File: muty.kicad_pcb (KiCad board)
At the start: 2 copper layers, 39 parts, among them J1 Conn_ARM_SWD_TagConnect_TC2030, J2 Conn_02x05_Odd_Even, U1 STM32F439ZITx, Y1 NX3215SA-32.768KHZ-EXS00A-MU0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, Y2 ECS-2520MVQ-160-CN-TR

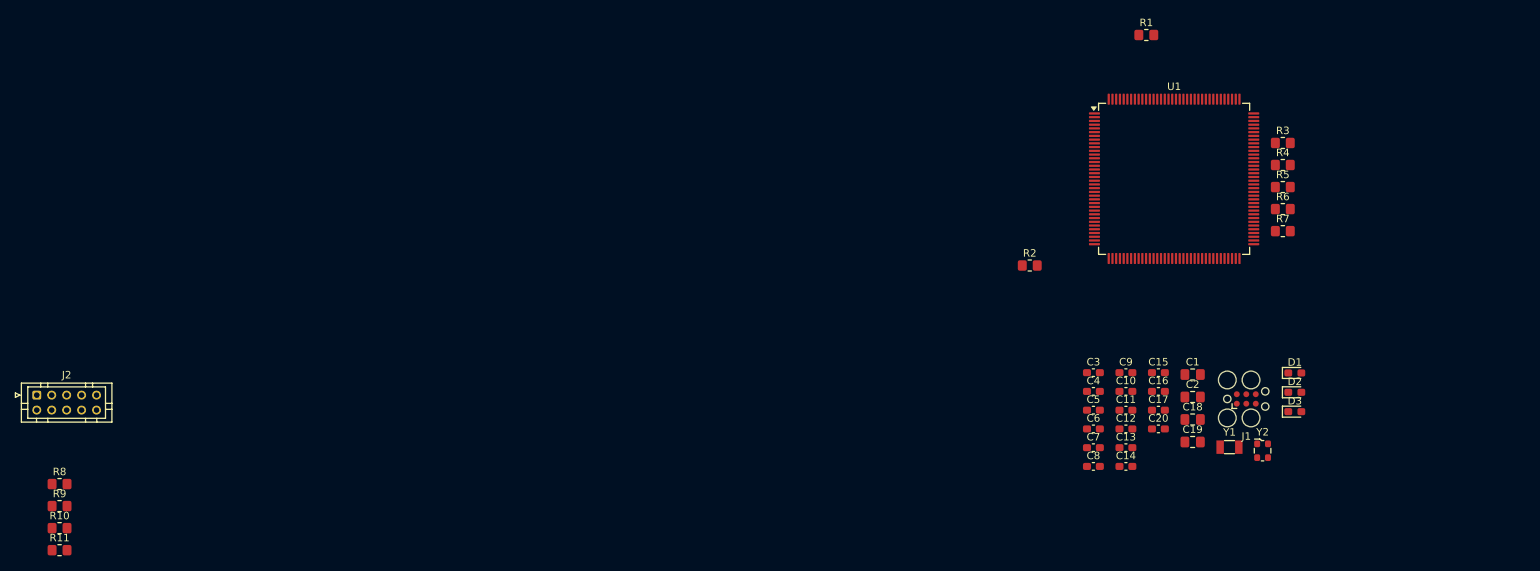
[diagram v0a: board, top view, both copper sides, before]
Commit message: feat: add bq25887 connector
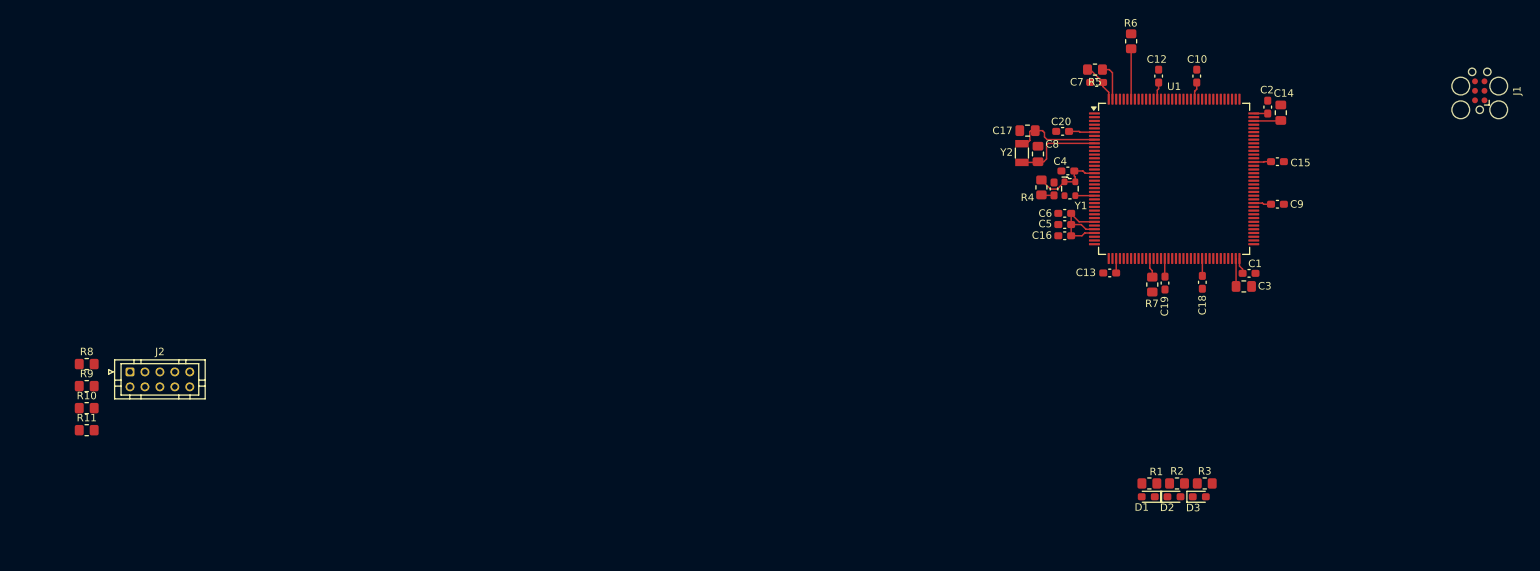
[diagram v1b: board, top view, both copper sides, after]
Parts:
- R11: value 900K -> 4,7K
- R9: value 4,7K -> 900K
- moved C10 53.1 mm to (207.8, 78.8), turned to -90 degrees
- moved J1 51.7 mm to (245.7, 80.8), turned to 90 degrees
- moved C12 50.5 mm to (202.8, 78.8), turned to -90 degrees
- moved C7 49.0 mm to (194.4, 79.7)
- moved Y2 48.2 mm to (184.4, 89.2), turned to -90 degrees
- moved C15 47.6 mm to (218.7, 90.3), turned to 180 degrees
- moved C14 45.6 mm to (219.1, 83.8), turned to -90 degrees
- moved C2 44.8 mm to (217.3, 83.0), turned to -90 degrees
- moved Y1 43.5 mm to (190.9, 93.9)
- moved R1 43.5 mm to (201.5, 133.4), turned to 180 degrees
- moved C17 41.9 mm to (185.2, 86.2)
- moved C20 39.5 mm to (189.9, 86.2)
- moved R2 39.4 mm to (205.2, 133.4)
- moved C9 37.0 mm to (218.7, 96.0), turned to 180 degrees
- moved C8 36.1 mm to (186.6, 89.3), turned to -90 degrees
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- renumbered C6 to C1, C14 to C10, C20 to C11, C7 to C12, C15 to C13, C19 to C14, C8 to C15, C2 to C17, C9 to C18, C10 to C19, C11 to C2, C17 to C20, C18 to C3, C3 to C4, C12 to C5, C4 to C6, C13 to C7, C1 to C8, C5 to C9, R5 to R1, R6 to R2, R7 to R3, R3 to R4, R4 to R5, R1 to R6, R2 to R7, Y2 to Y1, Y1 to Y2
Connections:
- R10 pad 2: BQ25887RGE_INT -> BQ25887RGE_SCL
- R11 pad 1: BQ25887RGE_CD -> +3.3V
- R11 pad 2: GND -> BQ25887RGE_INT
- R9 pad 1: +3.3V -> BQ25887RGE_CD
- R9 pad 2: BQ25887RGE_SCL -> GND
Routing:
- net +3.3V: track 0.00 -> 51.9 mm
- net RCC_LSE_OUT: track 0.00 -> 12.0 mm
- net RCC_LSE_IN: track 0.00 -> 12.0 mm
- net MCU_BOOT0: track 0.00 -> 6.75 mm
- net MCU_PDR_ON: track 0.00 -> 5.05 mm
- net VCAP1: track 0.00 -> 3.76 mm
- net VCAP2: track 0.00 -> 3.64 mm
- net RCC_HSE_IN: track 0.00 -> 2.67 mm
- net MCU_BOOT1: track 0.00 -> 2.62 mm
- net SWNRST: track 0.00 -> 1.72 mm
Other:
- copper layers 2 -> 4

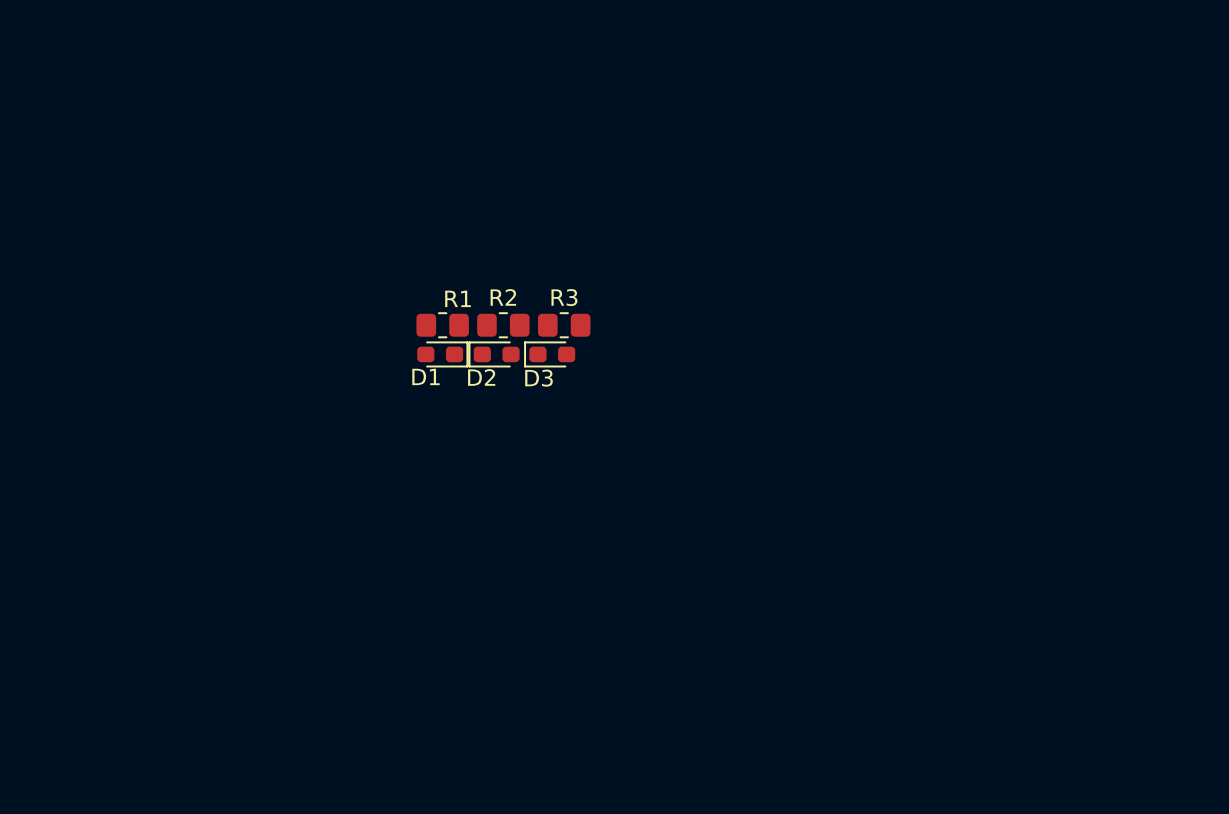
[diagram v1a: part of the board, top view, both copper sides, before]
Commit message: feat: add bno085+bme280
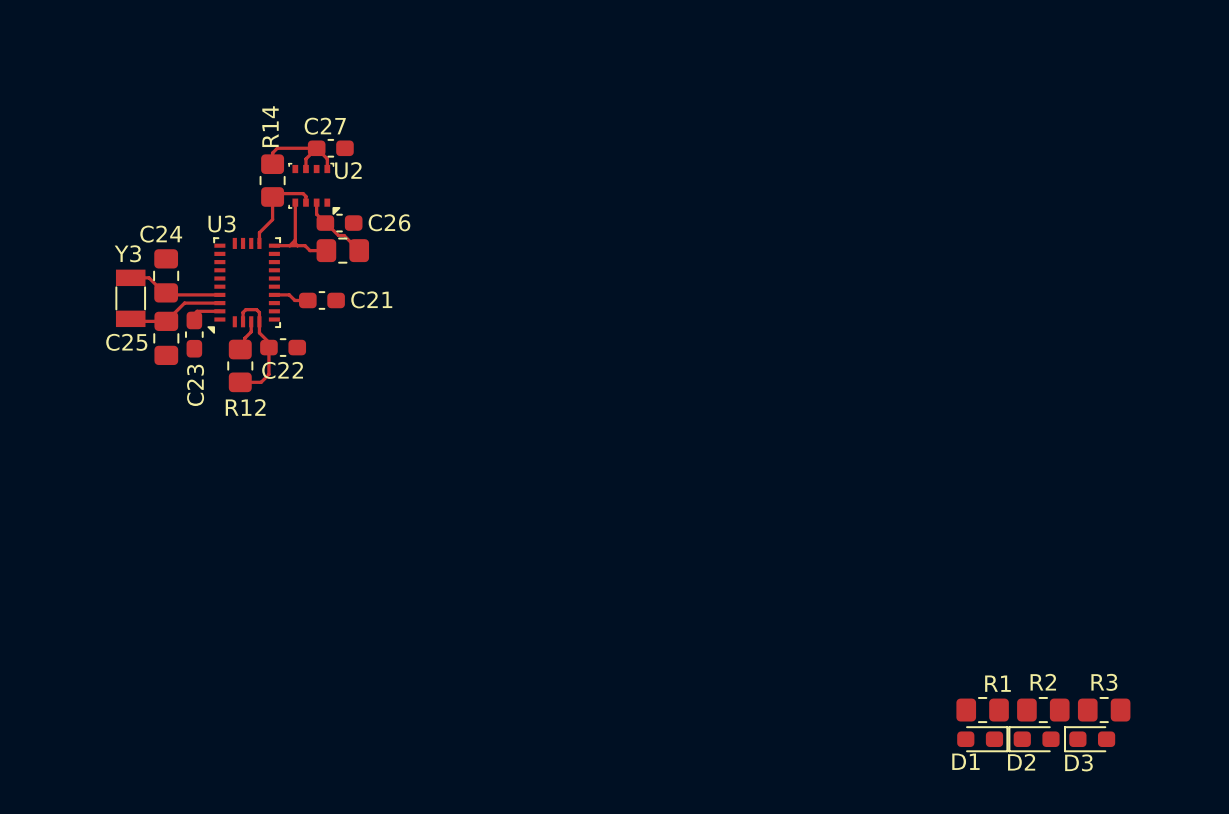
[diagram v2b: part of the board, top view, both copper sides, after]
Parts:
- added C21: 100nF, Capacitor_SMD:C_0603_1608Metric_Pad1.08x0.95mm_HandSolder, F.Cu at (194.2, 131.9)
- added C22: 100nF, Capacitor_SMD:C_0603_1608Metric_Pad1.08x0.95mm_HandSolder, F.Cu at (191.8, 134.7)
- added C23: 100nF, Capacitor_SMD:C_0603_1608Metric_Pad1.08x0.95mm_HandSolder, F.Cu at (186.4, 133.9)
- added C24: 22pF, Capacitor_SMD:C_0805_2012Metric_Pad1.18x1.45mm_HandSolder, F.Cu at (184.7, 130.4)
- added C25: 22pF, Capacitor_SMD:C_0805_2012Metric_Pad1.18x1.45mm_HandSolder, F.Cu at (184.7, 134.2)
- added C26: 100nF, Capacitor_SMD:C_0603_1608Metric_Pad1.08x0.95mm_HandSolder, F.Cu at (195.2, 127.1)
- added C27: 100nF, Capacitor_SMD:C_0603_1608Metric_Pad1.08x0.95mm_HandSolder, F.Cu at (194.7, 122.6)
- added R12: 10K, Resistor_SMD:R_0805_2012Metric_Pad1.20x1.40mm_HandSolder, F.Cu at (189.2, 135.8)
- added R13: 4,7K, Resistor_SMD:R_0805_2012Metric_Pad1.20x1.40mm_HandSolder, F.Cu at (195.4, 128.8)
- added R14: 4,7K, Resistor_SMD:R_0805_2012Metric_Pad1.20x1.40mm_HandSolder, F.Cu at (191.1, 124.5)
- added U2: BME280, Package_LGA:Bosch_LGA-8_2.5x2.5mm_P0.65mm_ClockwisePinNumbering, F.Cu at (193.5, 124.9)
- added U3: BNO085, Package_LGA:LGA-28_5.2x3.8mm_P0.5mm, F.Cu at (189.6, 130.8)
- added Y3: NX3215SA-32.768KHZ-EXS00A-MU00525, Crystal:Crystal_SMD_3215-2Pin_3.2x1.5mm, F.Cu at (182.5, 131.7)
- moved D1 40.4 mm to (234.3, 158.6)
- moved D3 40.4 mm to (241.1, 158.6)
- moved R1 40.4 mm to (234.4, 156.8)
- moved R3 40.4 mm to (241.8, 156.8)
- moved D2 40.4 mm to (237.7, 158.6)
- moved R2 40.4 mm to (238.1, 156.8)
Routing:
- net +3.3V: track 51.9 -> 72.4 mm
- net Net-(U2-SCK): track 0.00 -> 6.77 mm
- net Net-(U3-XIN32): track 0.00 -> 5.96 mm
- net Net-(U3-XOUT32): track 0.00 -> 5.87 mm
- net Net-(U2-SDI): track 0.00 -> 5.76 mm
- net Net-(U3-CAP): track 0.00 -> 2.18 mm
- net BNO085_BOOTN: track 0.00 -> 1.97 mm

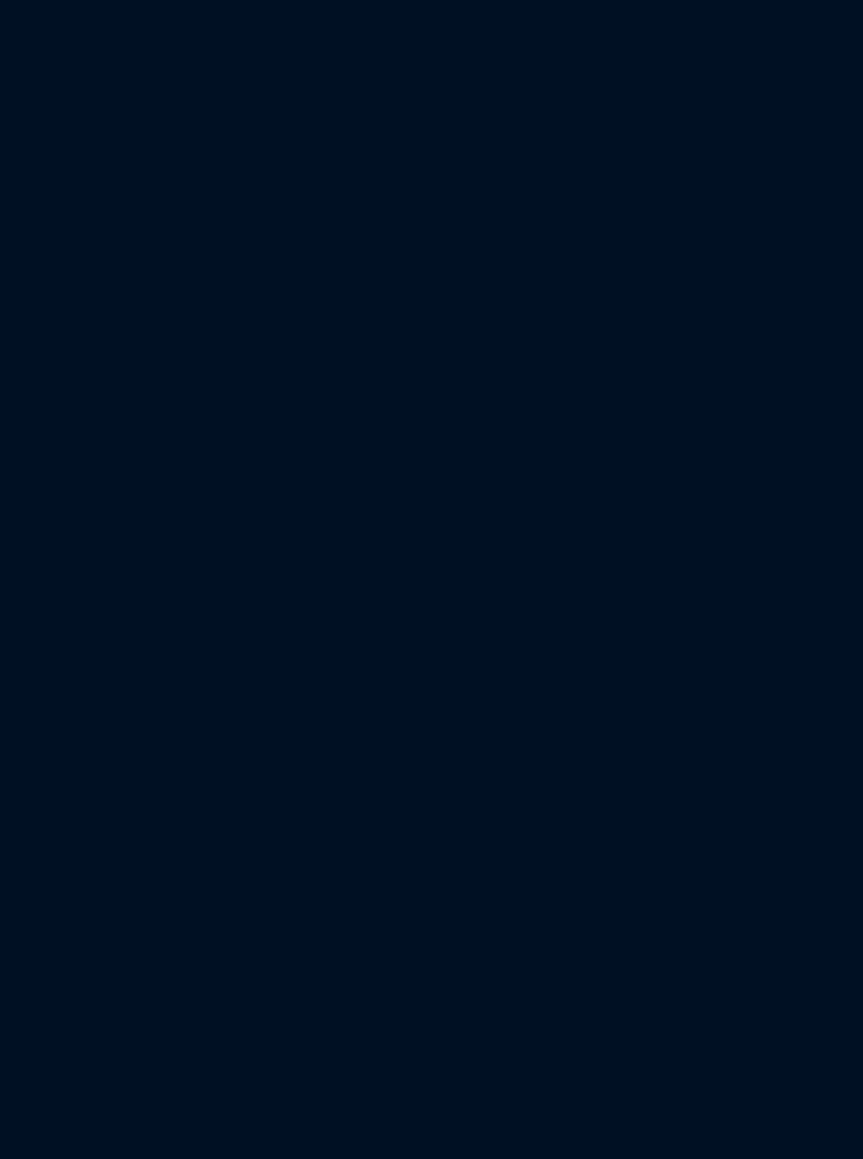
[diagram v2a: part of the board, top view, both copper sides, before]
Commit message: feat: add tb6612fng
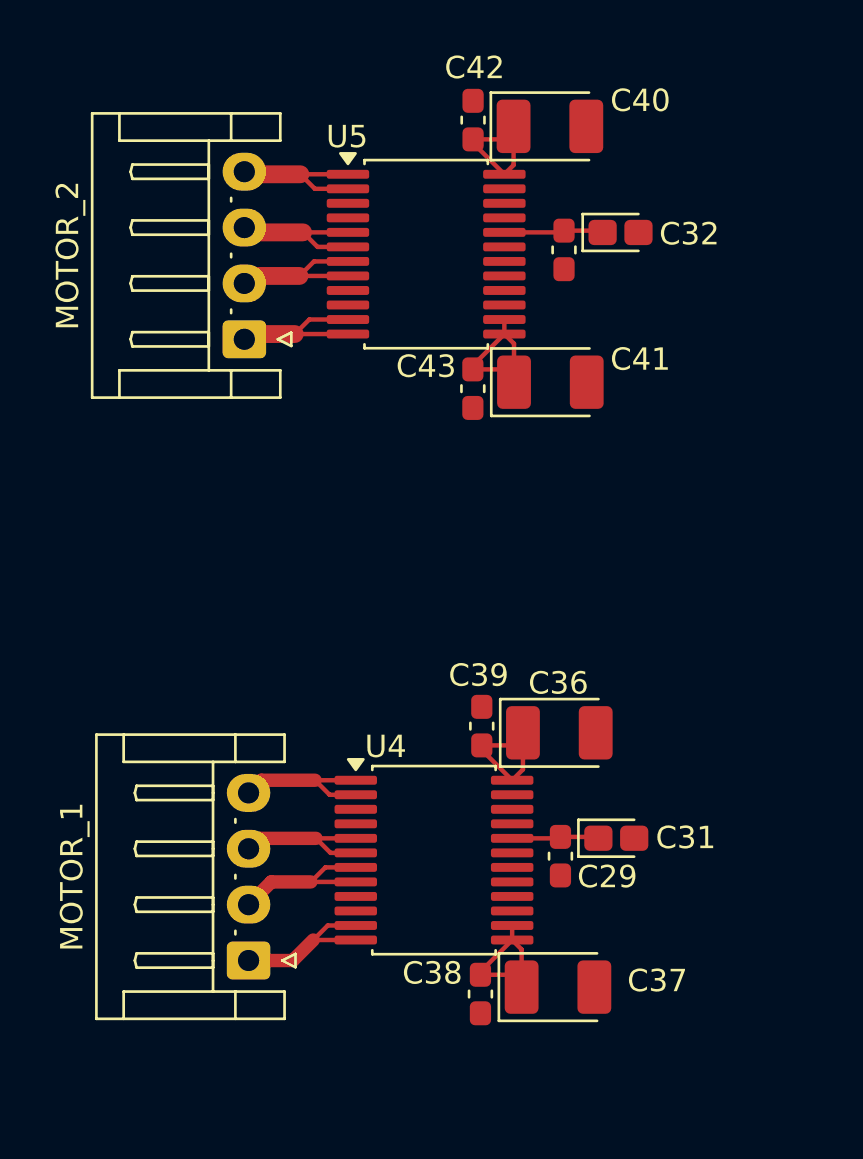
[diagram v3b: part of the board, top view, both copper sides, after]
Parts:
- added C29: 0.1μF, Capacitor_SMD:C_0603_1608Metric_Pad1.08x0.95mm_HandSolder, F.Cu at (46.3, 76.9)
- added C31: 10μF 10V, Capacitor_Tantalum_SMD:CP_EIA-1608-10_AVX-L_HandSolder, F.Cu at (48.8, 76.1)
- added C32: 10μF 10V, Capacitor_Tantalum_SMD:CP_EIA-1608-10_AVX-L_HandSolder, F.Cu at (49.0, 49.0)
- added C35: 0.1μF, Capacitor_SMD:C_0603_1608Metric_Pad1.08x0.95mm_HandSolder, F.Cu at (46.5, 49.8)
- added C36: 10μF 16V, Capacitor_Tantalum_SMD:CP_EIA-3528-15_AVX-H_HandSolder, F.Cu at (46.3, 71.4)
- added C37: 10μF 16V, Capacitor_Tantalum_SMD:CP_EIA-3528-15_AVX-H_HandSolder, F.Cu at (46.2, 82.8)
- added C38: 0.1μF, Capacitor_SMD:C_0603_1608Metric_Pad1.08x0.95mm_HandSolder, F.Cu at (42.8, 83.1)
- added C39: 0.1μF, Capacitor_SMD:C_0603_1608Metric_Pad1.08x0.95mm_HandSolder, F.Cu at (42.8, 71.1)
- added C40: 10μF 16V, Capacitor_Tantalum_SMD:CP_EIA-3528-15_AVX-H_HandSolder, F.Cu at (45.9, 44.2)
- added C41: 10μF 16V, Capacitor_Tantalum_SMD:CP_EIA-3528-15_AVX-H_HandSolder, F.Cu at (45.9, 55.7)
- added C42: 0.1μF, Capacitor_SMD:C_0603_1608Metric_Pad1.08x0.95mm_HandSolder, F.Cu at (42.4, 44.0)
- added C43: 0.1μF, Capacitor_SMD:C_0603_1608Metric_Pad1.08x0.95mm_HandSolder, F.Cu at (42.4, 56.0)
- added MOTOR_1: MOTOR_1X4, Connector_JST:JST_EH_S4B-EH_1x04_P2.50mm_Horizontal, F.Cu at (32.4, 81.6)
- added MOTOR_2: MOTOR_1X4, Connector_JST:JST_EH_S4B-EH_1x04_P2.50mm_Horizontal, F.Cu at (32.2, 53.8)
- added U4: TB6612FNG, Package_SO:SSOP-24_5.3x8.2mm_P0.65mm, F.Cu at (40.7, 77.1)
- added U5: TB6612FNG, Package_SO:SSOP-24_5.3x8.2mm_P0.65mm, F.Cu at (40.3, 50.0)
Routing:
- net +12V: track 0.00 -> 27.4 mm
- net M1_CHA2: track 0.00 -> 9.59 mm
- net M1_CHA1: track 0.00 -> 9.53 mm
- net +3.3V: track 72.4 -> 80.8 mm
- net M1_CHB1: track 0.00 -> 7.76 mm
- net M1_CHB2: track 0.00 -> 7.50 mm
- net M2_CHB1: track 0.00 -> 7.38 mm
- net M2_CHB2: track 0.00 -> 7.22 mm
- net M2_CHA1: track 0.00 -> 7.08 mm
- net M2_CHA2: track 0.00 -> 7.01 mm
